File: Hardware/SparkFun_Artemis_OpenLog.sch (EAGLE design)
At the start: 87 parts, among them J14 CORTEX_JTAG, J17 MICRO-SD, Q1 20V/0.2A/8MHz/1.2Ω/1Vth, Q10 20V/0.2A/8MHz/1.2Ω/1Vth, Q2 20V/4.2A/52mΩ/1.4W, Q3 20V/0.2A/8MHz/1.2Ω/1Vth, Q4 20V/4.2A/52mΩ/1.4W, Q7 20V/0.2A/8MHz/1.2Ω/1Vth, Q9 20V/0.2A/8MHz/1.2Ω/1Vth, U1 3.0V Supervisor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

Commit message: Add power down interrupt.
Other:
- note added: "0.65uA Leakage 0.3V drop at 10mA"
- note added: "300uA Leakage"
- note added: "Artemis"
- note added: "x04"
- note removed: "0.65uA / 0.3V drop at 10mA"
- note removed: "300uA"
- note removed: "Artemis (Apollo3)"
- note removed: "add mosfet power to SD card"
- note removed: "x02"
- moved on the sheet: C46, Q2
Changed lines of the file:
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@@
 Vdrop (max): 250mV
 Iq: 55uA</text>
-<text x="421.64" y="7.62" size="2.54" layer="94">x02</text>
+<text x="421.64" y="7.62" size="2.54" layer="94">x04</text>
 <text x="355.6" y="11.43" size="2.54" layer="94">N. Seidle</text>
 <wire x1="0" y1="210.82" x2="111.76" y2="210.82" width="0.254" layer="97" style="longdash"/>
@@
 (1000V/Rprog)</text>
 <text x="129.794" y="153.416" size="2.54" layer="97" align="center">SWD Program/Debug Interface</text>
-<text x="88.9" y="106.68" size="2.54" layer="97" align="center">Artemis (Apollo3)</text>
+<text x="88.9" y="106.68" size="2.54" layer="97" align="center">Artemis</text>
 <text x="83.82" y="96.52" size="1.778" layer="97">Artemis VCC Range:
 1.76-3.6V</text>
@@
 <text x="48.514" y="271.526" size="2.54" layer="97" font="vector" align="center">USB-to-Serial Converter</text>
 <text x="221.234" y="197.866" size="2.54" layer="97" font="vector" align="center">Bootloader Reset Circuit</text>
-<text x="347.98" y="195.58" size="2.54" layer="97" align="center">μSD</text>
+<text x="342.9" y="198.12" size="2.54" layer="97" align="center">μSD</text>
 <text x="243.84" y="40.64" size="2.54" layer="97" font="vector" align="center">ICM-20948 IMU</text>
 <text x="208.28" y="81.28" size="2.54" layer="97" font="vector" align="center">Voltage Regulator</text>
@@
 <wire x1="60.96" y1="167.64" x2="60.96" y2="210.82" width="0.254" layer="97" style="longdash"/>
 <wire x1="297.18" y1="144.78" x2="297.18" y2="210.82" width="0.254" layer="97" style="longdash"/>
-<text x="33.528" y="139.192" size="1.27" layer="91" rot="R90">300uA</text>
-<text x="9.652" y="137.922" size="1.27" layer="91" rot="R90">0.65uA / 0.3V drop at 10mA</text>
-<text x="452.12" y="162.56" size="1.27" layer="91">add mosfet power to SD card</text>
+<text x="33.02" y="132.08" size="1.778" layer="97" rot="R90">300uA Leakage</text>
+<text x="12.7" y="139.7" size="1.778" layer="97" rot="R90">0.65uA Leakage
+0.3V drop at 10mA</text>
 <text x="152.4" y="93.98" size="1.27" layer="91">SD_PWR: 23</text>
 <text x="149.86" y="91.44" size="1.27" layer="91">x04:</text>
@@
 <attribute name="VALUE" x="345.44" y="157.48" size="1.778" layer="96"/>
 </instance>
-<instance part="C46" gate="G$1" x="327.66" y="167.64" smashed="yes">
-<attribute name="NAME" x="329.184" y="170.561" size="1.778" layer="95" font="vector"/>
-<attribute name="VALUE" x="329.184" y="165.481" size="1.778" layer="96" font="vector"/>
-</instance>
-<instance part="GND73" gate="1" x="327.66" y="160.02" smashed="yes">
-<attribute name="VALUE" x="327.66" y="159.766" size="1.778" layer="96" align="top-center"/>
+<instance part="C46" gate="G$1" x="325.12" y="167.64" smashed="yes">
+<attribute name="NAME" x="326.644" y="170.561" size="1.778" layer="95" font="vector"/>
+<attribute name="VALUE" x="326.644" y="165.481" size="1.778" layer="96" font="vector"/>
+</instance>
+<instance part="GND73" gate="1" x="325.12" y="160.02" smashed="yes">
+<attribute name="VALUE" x="325.12" y="159.766" size="1.778" layer="96" align="top-center"/>
 </instance>
 <instance part="U13" gate="G$1" x="243.84" y="22.86" smashed="yes">
@@
 <instance part="D3" gate="G$1" x="25.4" y="142.24" smashed="yes" rot="R90">
 <attribute name="NAME" x="28.448" y="139.7" size="1.778" layer="95" font="vector" rot="R90"/>
-<attribute name="VALUE" x="31.242" y="152.4" size="1.778" layer="96" font="vector" rot="R270" align="top-left"/>
+<attribute name="VALUE" x="30.48" y="132.08" size="1.778" layer="96" font="vector" rot="MR90" align="top-left"/>
 </instance>
 <instance part="R1" gate="G$1" x="17.78" y="142.24" smashed="yes" rot="MR90">
@@
 <instance part="D6" gate="G$1" x="17.78" y="154.94" smashed="yes" rot="R270">
 <attribute name="NAME" x="14.224" y="156.718" size="1.778" layer="95" font="vector" rot="R270"/>
-<attribute name="VALUE" x="13.716" y="162.052" size="1.778" layer="96" font="vector" rot="R270" align="top-left"/>
+<attribute name="VALUE" x="7.62" y="139.7" size="1.778" layer="96" font="vector" rot="MR90" align="top-left"/>
 </instance>
 <instance part="C5" gate="G$1" x="149.86" y="185.42" smashed="yes">
@@
 <attribute name="VALUE" x="160.02" y="177.546" size="1.778" layer="96" rot="MR0" align="top-center"/>
 </instance>
-<instance part="Q2" gate="G$1" x="325.12" y="185.42" smashed="yes" rot="MR180">
-<attribute name="NAME" x="330.2" y="190.5" size="1.778" layer="95" font="vector" rot="MR180"/>
-<attribute name="VALUE" x="330.2" y="193.04" size="1.778" layer="96" font="vector" rot="MR180"/>
-</instance>
-<instance part="SUPPLY15" gate="G$1" x="327.66" y="193.04" smashed="yes">
-<attribute name="VALUE" x="327.66" y="195.834" size="1.778" layer="96" align="bottom-center"/>
+<instance part="Q2" gate="G$1" x="322.58" y="185.42" smashed="yes" rot="MR180">
+<attribute name="NAME" x="327.66" y="190.5" size="1.778" layer="95" font="vector" rot="MR180"/>
+<attribute name="VALUE" x="327.66" y="193.04" size="1.778" layer="96" font="vector" rot="MR180"/>
+</instance>
+<instance part="SUPPLY15" gate="G$1" x="325.12" y="193.04" smashed="yes">
+<attribute name="VALUE" x="325.12" y="195.834" size="1.778" layer="96" align="bottom-center"/>
 </instance>
 </instances>
@@
 <pinref part="C46" gate="G$1" pin="2"/>
 <pinref part="GND73" gate="1" pin="GND"/>
-<wire x1="327.66" y1="162.56" x2="327.66" y2="165.1" width="0.1524" layer="91"/>
+<wire x1="325.12" y1="162.56" x2="325.12" y2="165.1" width="0.1524" layer="91"/>
 </segment>
 <segment>
@@
 <pinref part="Q2" gate="G$1" pin="S"/>
 <pinref part="SUPPLY15" gate="G$1" pin="3.3V"/>
-<wire x1="327.66" y1="193.04" x2="327.66" y2="190.5" width="0.1524" layer="91"/>
+<wire x1="325.12" y1="193.04" x2="325.12" y2="190.5" width="0.1524" layer="91"/>
 </segment>
 </net>
@@
 <segment>
 <pinref part="Q2" gate="G$1" pin="G"/>
-<wire x1="320.04" y1="187.96" x2="317.5" y2="187.96" width="0.1524" layer="91"/>
-<label x="317.5" y="187.96" size="1.27" layer="95" rot="R180" xref="yes"/>
+<wire x1="317.5" y1="187.96" x2="314.96" y2="187.96" width="0.1524" layer="91"/>
+<label x="314.96" y="187.96" size="1.27" layer="95" rot="R180" xref="yes"/>
 </segment>
 <segment>
@@
 <net name="SD_PWR" class="0">
 <segment>
-<wire x1="342.9" y1="177.8" x2="327.66" y2="177.8" width="0.1524" layer="91"/>
+<wire x1="342.9" y1="177.8" x2="325.12" y2="177.8" width="0.1524" layer="91"/>
 <pinref part="J17" gate="J1" pin="VCC"/>
 <pinref part="C46" gate="G$1" pin="1"/>
-<wire x1="327.66" y1="172.72" x2="327.66" y2="177.8" width="0.1524" layer="91"/>
-<junction x="327.66" y="177.8"/>
+<wire x1="325.12" y1="172.72" x2="325.12" y2="177.8" width="0.1524" layer="91"/>
+<junction x="325.12" y="177.8"/>
 <pinref part="Q2" gate="G$1" pin="D"/>
-<wire x1="327.66" y1="180.34" x2="327.66" y2="177.8" width="0.1524" layer="91"/>
-</segment>
-</net>
+<wire x1="325.12" y1="180.34" x2="325.12" y2="177.8" width="0.1524" layer="91"/>
+</segment>
+</net>

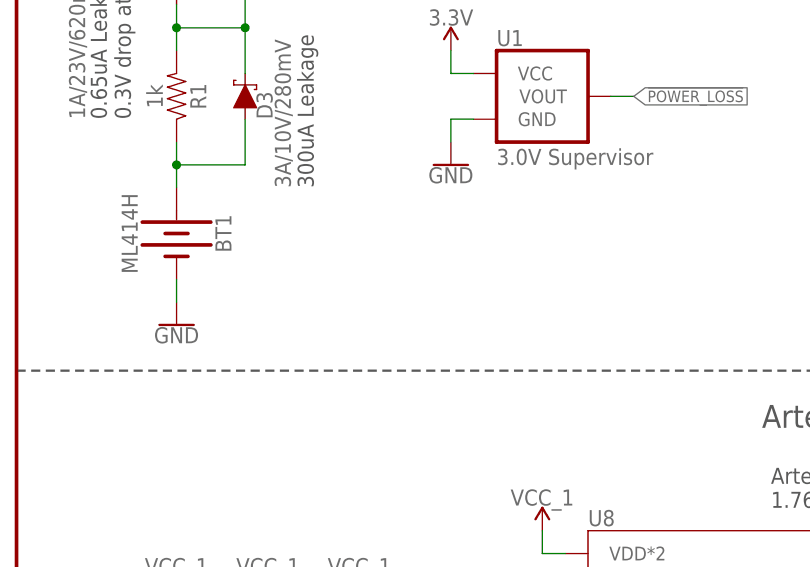
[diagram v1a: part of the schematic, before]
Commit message: Enter low power mode and maintain RTC at ~3.00uA.
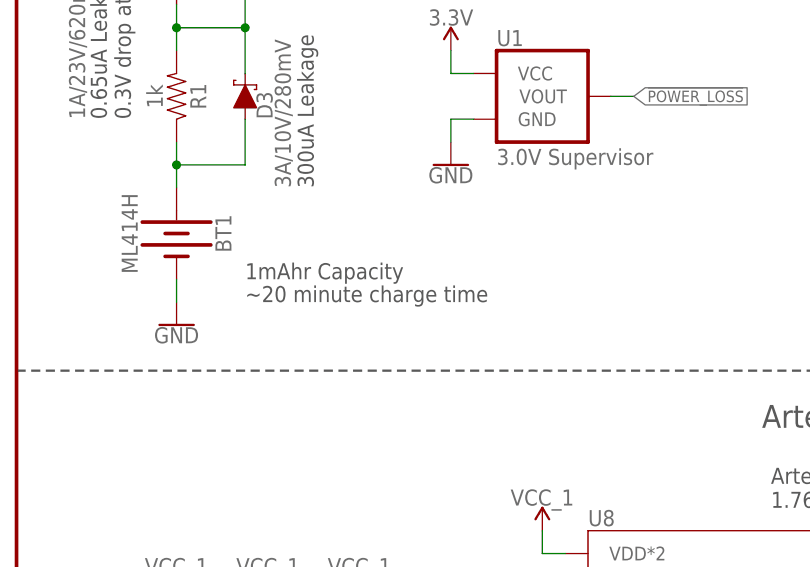
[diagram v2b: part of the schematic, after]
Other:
- note added: "1mAhr Capacity"
- note added: "~20 minute charge time"
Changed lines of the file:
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@@
 <text x="152.4" y="93.98" size="1.27" layer="91">SD_PWR: 23</text>
 <text x="149.86" y="91.44" size="1.27" layer="91">x04:</text>
+<text x="25.4" y="119.38" size="1.778" layer="97">~20 minute charge time</text>
+<text x="25.4" y="121.92" size="1.778" layer="97">1mAhr Capacity</text>
 </plain>
 <instances>

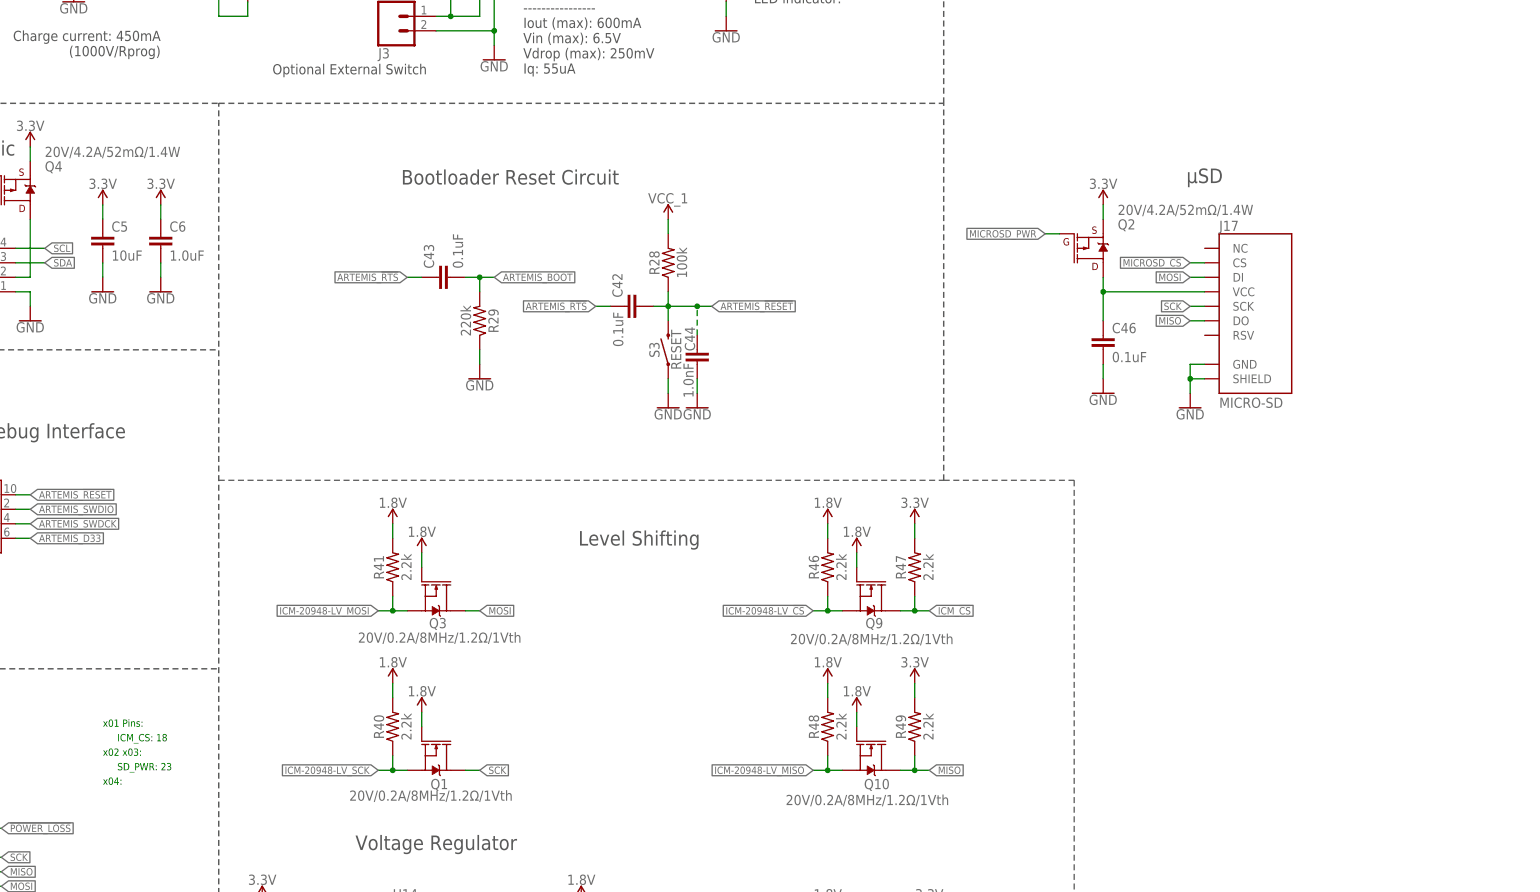
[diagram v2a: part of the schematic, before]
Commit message: Add dimension and schematic PDFs. Add readme and issue_template.
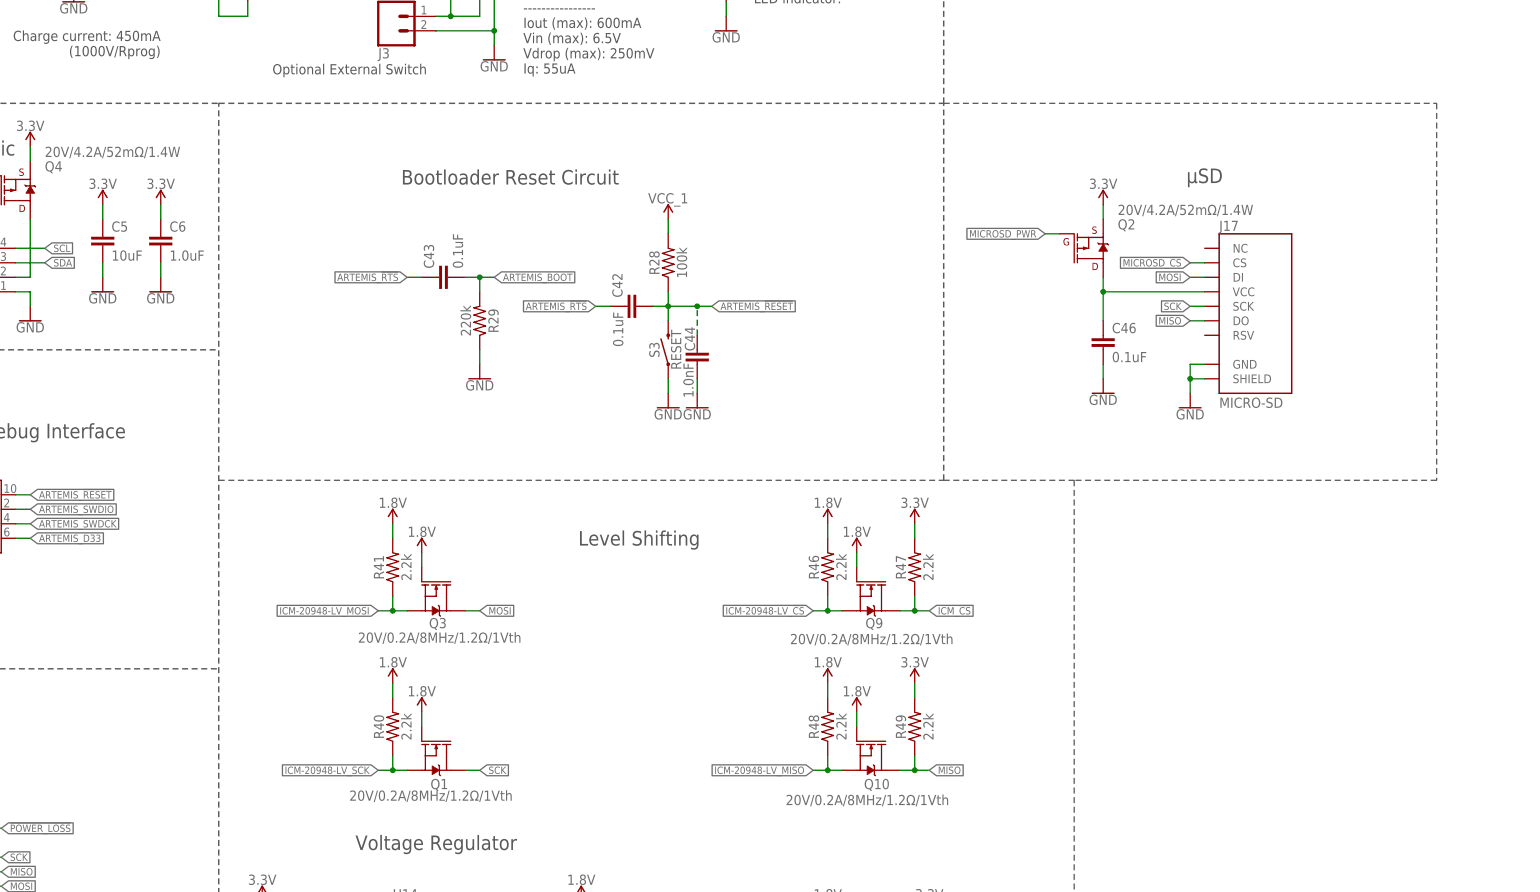
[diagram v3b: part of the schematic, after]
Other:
- note removed: "ICM_CS: 18"
- note removed: "SD_PWR: 23"
- note removed: "x01 Pins:"
- note removed: "x02 x03:"
- note removed: "x04:"
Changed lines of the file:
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@@
 <?xml version="1.0" encoding="utf-8"?>
 <!DOCTYPE eagle SYSTEM "eagle.dtd">
-<eagle version="9.5.2">
+<eagle version="9.6.0">
 <drawing>
 <settings>
@@
 <wire x1="297.18" y1="144.78" x2="320.04" y2="144.78" width="0.2032" layer="97" style="longdash"/>
 <text x="130.302" y="202.946" size="2.54" layer="97" font="vector" rot="R180" align="center">Qwiic</text>
-<text x="149.86" y="101.6" size="1.27" layer="91">x01 Pins:</text>
-<text x="149.86" y="96.52" size="1.27" layer="91">x02 x03:</text>
-<text x="152.4" y="99.06" size="1.27" layer="91">ICM_CS: 18</text>
 <text x="51.054" y="162.306" size="2.54" layer="97" font="vector" align="center">RTC Battery</text>
 <text x="179.578" y="215.9" size="1.778" layer="97" font="vector">Optional External Switch</text>
@@
 <text x="12.7" y="139.7" size="1.778" layer="97" rot="R90">0.65uA Leakage
 0.3V drop at 10mA</text>
-<text x="152.4" y="93.98" size="1.27" layer="91">SD_PWR: 23</text>
-<text x="149.86" y="91.44" size="1.27" layer="91">x04:</text>
 <text x="25.4" y="119.38" size="1.778" layer="97">~20 minute charge time</text>
 <text x="25.4" y="121.92" size="1.778" layer="97">1mAhr Capacity</text>
+<wire x1="297.18" y1="210.82" x2="383.54" y2="210.82" width="0.2032" layer="97" style="longdash"/>
+<wire x1="383.54" y1="210.82" x2="383.54" y2="144.78" width="0.2032" layer="97" style="longdash"/>
+<wire x1="383.54" y1="144.78" x2="320.04" y2="144.78" width="0.2032" layer="97" style="longdash"/>
 </plain>
 <instances>
